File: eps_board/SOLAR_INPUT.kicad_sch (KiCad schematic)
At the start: 1 part, among them J1 Conn_01x04

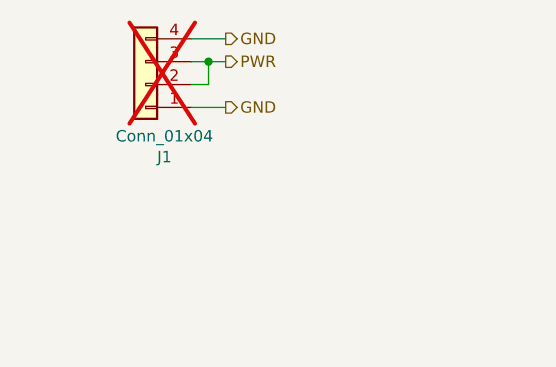
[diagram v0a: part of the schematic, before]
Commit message: EPS use M50 2x3 connectors for solar cells. remove 2 connectors since they are all tied together and top/bottom can be routed through sides and side connectors
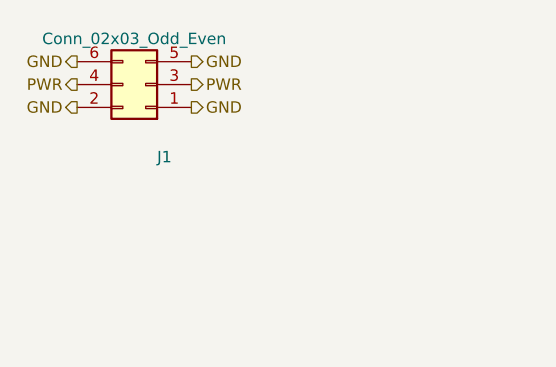
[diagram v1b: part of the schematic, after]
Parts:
- J1: value Conn_01x04 -> Conn_02x03_Odd_Even; footprint Connector_PinHeader_2.54mm:PinHeader_1x04_P2.54mm_Vertical -> Common:HARWIN_M50-3200345; symbol Connector_Generic:Conn_01x04 -> Connector_Generic:Conn_02x03_Odd_Even; Manufacturer (none) -> Harwin; Part Number (none) -> M50-3200345; now fitted
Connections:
- net GND: now also J1.2 (Pin_2), J1.5 (Pin_5), J1.6 (Pin_6); no longer J1.4 (Pin_4)
- net PWR: now also J1.4 (Pin_4); no longer J1.2 (Pin_2)
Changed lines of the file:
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@@
 		(date "2020-08-09")
-	)
-	(junction
-		(at 144.145 95.885)
-		(diameter 0)
-		(color 0 0 0 0)
-	)
-	(wire
-		(pts
-			(xy 144.145 95.885) (xy 144.145 98.425)
-		)
-		(stroke
-			(width 0)
-			(type default)
-		)
-	)
-	(wire
-		(pts
-			(xy 144.145 95.885) (xy 146.05 95.885)
-		)
-		(stroke
-			(width 0)
-			(type default)
-		)
-	)
-	(wire
-		(pts
-			(xy 142.24 100.965) (xy 146.05 100.965)
-		)
-		(stroke
-			(width 0)
-			(type default)
-		)
-	)
-	(wire
-		(pts
-			(xy 142.24 98.425) (xy 144.145 98.425)
-		)
-		(stroke
-			(width 0)
-			(type default)
-		)
-	)
-	(wire
-		(pts
-			(xy 142.24 95.885) (xy 144.145 95.885)
-		)
-		(stroke
-			(width 0)
-			(type default)
-		)
-	)
-	(wire
-		(pts
-			(xy 142.24 93.345) (xy 146.05 93.345)
-		)
-		(stroke
-			(width 0)
-			(type default)
-		)
 	)
 	(text "I used to use Molex Pico Lock:\n5040500491\nhttps://www.digikey.com/en/products/detail/molex/5040500491/4357649\n"
@@
 	(hierarchical_label "GND"
 		(shape output)
-		(at 146.05 93.345 0)
+		(at 142.24 95.885 0)
 		(fields_autoplaced yes)
 		(effects
@@
 	(hierarchical_label "GND"
 		(shape output)
-		(at 146.05 100.965 0)
+		(at 142.24 100.965 0)
 		(fields_autoplaced yes)
 		(effects
@@
 		)
 	)
+	(hierarchical_label "GND"
+		(shape output)
+		(at 129.54 95.885 180)
+		(fields_autoplaced yes)
+		(effects
+			(font
+				(size 1.27 1.27)
+			)
+			(justify right)
+		)
+	)
+	(hierarchical_label "GND"
+		(shape output)
+		(at 129.54 100.965 180)
+		(fields_autoplaced yes)
+		(effects
+			(font
+				(size 1.27 1.27)
+			)
+			(justify right)
+		)
+	)
 	(hierarchical_label "PWR"
 		(shape output)
-		(at 146.05 95.885 0)
+		(at 129.54 98.425 180)
+		(fields_autoplaced yes)
+		(effects
+			(font
+				(size 1.27 1.27)
+			)
+			(justify right)
+		)
+	)
+	(hierarchical_label "PWR"
+		(shape output)
+		(at 142.24 98.425 0)
 		(fields_autoplaced yes)
 		(effects
@@
 	)
 	(symbol
-		(lib_id "Connector_Generic:Conn_01x04")
+		(lib_id "Connector_Generic:Conn_02x03_Odd_Even")
 		(at 137.16 98.425 180)
 		(unit 1)
@@
 		(in_bom yes)
 		(on_board yes)
-		(dnp yes)
+		(dnp no)
 		(property "Reference" "J1"
 			(at 139.2428 106.4768 0)
@@
 			)
 		)
-		(property "Value" "Conn_01x04"
-			(at 139.2428 104.1654 0)
+		(property "Value" "Conn_02x03_Odd_Even"
+			(at 135.89 93.345 0)
 			(effects
 				(font
@@
 			)
 		)
-		(property "Footprint" "Connector_PinHeader_2.54mm:PinHeader_1x04_P2.54mm_Vertical"
+		(property "Footprint" "Common:HARWIN_M50-3200345"
 			(at 137.16 98.425 0)
 			(effects
@@
 			)
 		)
-		(property "Datasheet" "~"
+		(property "Datasheet" "https://cdn.harwin.com/pdfs/M50-320.pdf"
 			(at 137.16 98.425 0)
 			(effects
@@
 			)
 		)
-		(property "Description" ""
+		(property "Description" "Generic connector, double row, 02x03, odd/even pin numbering scheme (row 1 odd numbers, row 2 even numbers), script generated (kicad-library-utils/schlib/autogen/connector/)"
+			(at 137.16 98.425 0)
+			(effects
+				(font
+					(size 1.27 1.27)
+				)
+				(hide yes)
+			)
+		)
+		(property "Manufacturer" "Harwin"
+			(at 137.16 98.425 0)
+			(effects
+				(font
+					(size 1.27 1.27)
+				)
+				(hide yes)
+			)
+		)
+		(property "Part Number" "M50-3200345"
 			(at 137.16 98.425 0)
 			(effects
@@
 		)
 		(pin "4"
+		)
+		(pin "6"
+		)
+		(pin "5"
 		)
 		(instances
@@
 					(unit 1)
 				)
-				(path "/05170af6-30ef-4c3a-b972-f098085da1bc/00000000-0000-0000-0000-000061679a36"
-					(reference "J5")
-					(unit 1)
-				)
-				(path "/05170af6-30ef-4c3a-b972-f098085da1bc/00000000-0000-0000-0000-0000616870b5"
-					(reference "J6")
-					(unit 1)
-				)
